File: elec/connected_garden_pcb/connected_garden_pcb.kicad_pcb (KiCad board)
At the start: 2 copper layers, 21 parts, among them J1 Moisture1, J2 Moisture2, J3 Moisture3, J4 Moisture4, J5 Moisture5, J6 Screw_Terminal_01x02, J7 UART out, SW1 Reset, SW2 Flash, U1 TP4056-18650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

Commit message: Changes MCP3208 footprint, reroute and add text
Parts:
- U2: footprint Package_DIP:DIP-16_W7.62mm_Socket_LongPads -> Package_SO:SOIC-16_3.9x9.9mm_P1.27mm
- moved U2 11.4 mm to (40.6, 68.6)
- moved J1 3.17 mm to (26.2, 82.7)
- moved J2 3.17 mm to (32.3, 82.7)
- moved J4 3.17 mm to (44.6, 82.7)
- moved J5 3.17 mm to (50.8, 82.7)
- moved J3 3.10 mm to (38.6, 82.8)
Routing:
- net /CS: track 30.4 -> 14.8 mm, vias 0 -> 2
- net GND: track 202.1 -> 195.4 mm
- net +3V3: track 173.5 -> 167.5 mm
- net /A5: track 98.1 -> 92.8 mm
- net /A0: track 7.94 -> 12.9 mm
- net /A1: track 6.45 -> 8.57 mm
- net /SCLK: track 13.0 -> 14.4 mm, vias 1 -> 2
- net /A3: track 9.53 -> 8.29 mm
- net /MOSI: track 7.12 -> 6.07 mm
- net /MISO: track 8.79 -> 7.81 mm
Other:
- board text added: "1"
- board text added: "2"
- board text added: "3"
- board text added: "3V3"
- board text added: "4"
- board text added: "5"
- board text added: "Connected Garden V1 By Guilhem B."
- board text added: "DHT11"
- board text added: "Flash"
- board text added: "GND"
- board text added: "Moisture Sensors"
- board text added: "Panel"
- board text added: "RX"
- board text added: "Reset"
- board text added: "SIG"
- board text added: "TX"

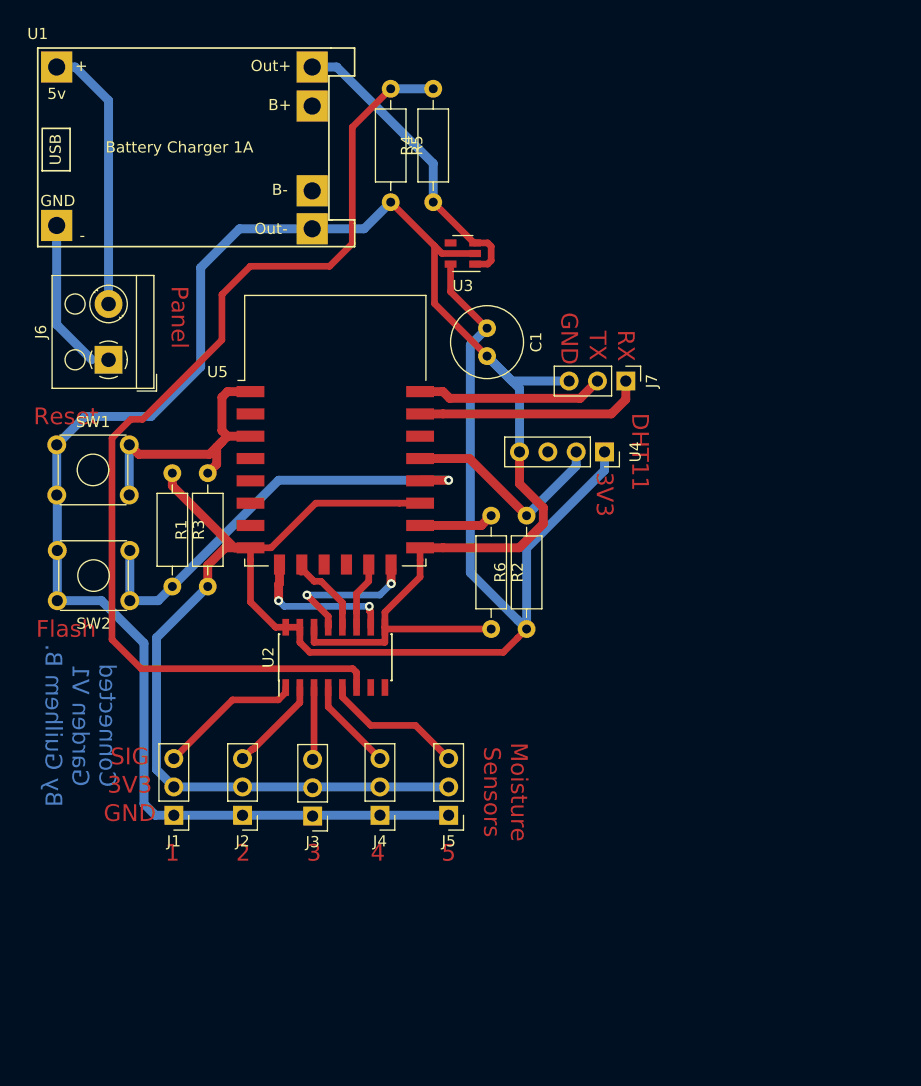
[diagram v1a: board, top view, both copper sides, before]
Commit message: [Elec] Reroutes PCB to v1.2
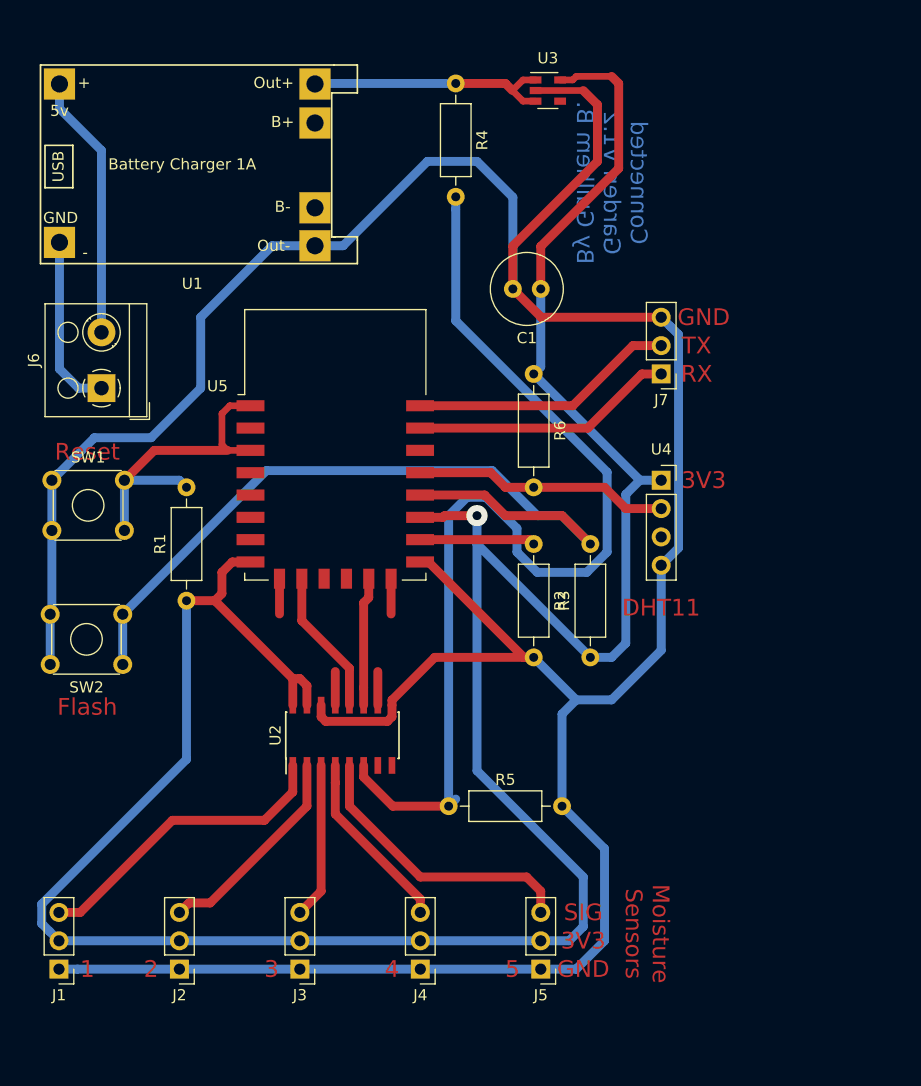
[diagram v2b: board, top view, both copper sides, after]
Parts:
- moved R5 64.5 mm to (50.8, 81.9), turned to 0 degrees
- moved R3 40.9 mm to (63.5, 68.6), turned to 90 degrees
- moved R6 22.9 mm to (58.4, 43.2), turned to 270 degrees
- moved J1 17.2 mm to (15.9, 96.5)
- moved U3 16.5 mm to (59.7, 17.8), turned to 0 degrees
- moved J5 16.1 mm to (59.1, 96.5)
- moved J2 14.9 mm to (26.7, 96.5)
- moved J4 14.3 mm to (48.3, 96.5)
- moved J3 13.8 mm to (37.5, 96.5)
- moved R4 10.8 mm to (51.4, 17.1), turned to 270 degrees
- moved U2 7.01 mm to (41.3, 75.6)
- moved C1 5.96 mm to (59.1, 35.6), turned to 180 degrees
- moved SW2 5.75 mm to (21.6, 69.2)
- moved U4 5.68 mm to (69.8, 52.7), turned to 0 degrees
- moved R2 4.58 mm to (58.4, 58.4)
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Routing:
- net GND: track 195.4 -> 279.9 mm
- net +3V3: track 167.5 -> 237.2 mm, vias 0 -> 1
- net Net-(R3-Pad2): track 40.1 -> 71.5 mm, vias 1 -> 0
- net /A0: track 12.9 -> 27.8 mm
- net /A4: track 12.7 -> 25.9 mm
- net /A1: track 8.57 -> 19.0 mm
- net /CS: track 14.8 -> 6.17 mm, vias 2 -> 0
- net /SCLK: track 14.4 -> 6.17 mm, vias 2 -> 0
- net /A3: track 8.29 -> 16.3 mm
- net /A2: track 6.50 -> 14.0 mm
- net /TX: track 16.8 -> 23.8 mm
- net /MOSI: track 6.07 -> 11.5 mm
- net /MISO: track 7.81 -> 13.1 mm
- net Net-(R4-Pad1): track 27.6 -> 22.9 mm
- net /DHT11Data: track 19.2 -> 22.9 mm
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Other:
- net class Default: trace_width 0.25 -> 0.6; via_dia 0.8 -> 1.9; via_drill 0.4 -> 0.8
- rule trace_min: 0.2 -> 0.6
- board text added: "Connected Garden V1.2 By Guilhem B."
- board text removed: "Connected Garden V1 By Guilhem B."
- board text removed: "Panel"

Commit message: [Elec] Routes the new BUZ11
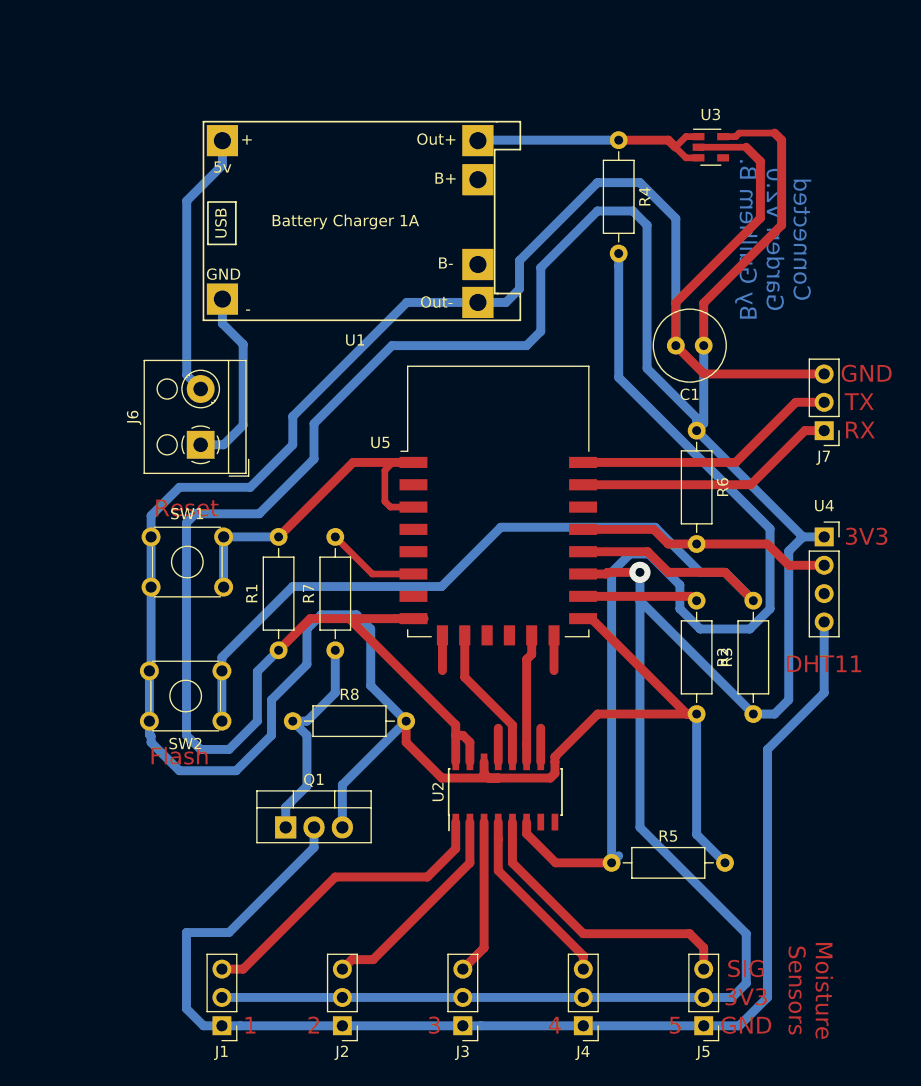
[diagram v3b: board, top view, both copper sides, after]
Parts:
- added Q1: BUZ11, Package_TO_SOT_THT:TO-220-3_Vertical, F.Cu at (36.2, 83.8)
- added R7: 220, Resistor_THT:R_Axial_DIN0207_L6.3mm_D2.5mm_P10.16mm_Horizontal, F.Cu at (40.6, 67.9)
- added R8: 10K, Resistor_THT:R_Axial_DIN0207_L6.3mm_D2.5mm_P10.16mm_Horizontal, F.Cu at (36.8, 74.3)
- moved J4 15.5 mm to (62.9, 101.6)
- moved J7 15.5 mm to (84.5, 48.3)
- moved R2 15.5 mm to (73.0, 63.5)
- moved R3 15.5 mm to (78.1, 73.7)
- moved R4 15.5 mm to (66.0, 22.2)
- moved R5 15.5 mm to (65.4, 87.0)
- moved R6 15.5 mm to (73.0, 48.3)
- moved U2 15.5 mm to (55.9, 80.6)
- moved U3 15.5 mm to (74.3, 22.9)
- moved U4 15.5 mm to (84.5, 57.8)
- moved J1 15.5 mm to (30.5, 101.6)
- moved U1 15.5 mm to (28.8, 20.6)
- moved C1 15.5 mm to (73.7, 40.6)
- moved J2 15.5 mm to (41.3, 101.6)
- moved J3 15.5 mm to (52.1, 101.6)
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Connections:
- J1 pad 1: GND -> /GND_EN
- J2 pad 1: GND -> /GND_EN
- J3 pad 1: GND -> /GND_EN
- J4 pad 1: GND -> /GND_EN
- J5 pad 1: GND -> /GND_EN
- U4 pad 4: GND -> /GND_EN
- U5 pad 6: Net-(U5-Pad6) -> /MOSG
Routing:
- net /GND_EN: track 0.00 -> 112.7 mm
- net +3V3: track 237.2 -> 325.6 mm
- net GND: track 279.9 -> 250.9 mm
- net Net-(Q1-Pad1): track 0.00 -> 19.5 mm
- net /MOSG: track 0.00 -> 8.38 mm
- net Net-(R3-Pad2): track 71.5 -> 78.0 mm
- net Net-(R1-Pad2): track 29.1 -> 32.7 mm
- net Net-(J6-Pad1): track 15.8 -> 16.6 mm
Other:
- board text added: "Connected Garden V2.0 By Guilhem B."
- board text removed: "Connected Garden V1.2 By Guilhem B."
